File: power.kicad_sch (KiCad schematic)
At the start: 50 parts, among them J5 Ride Through, Q12 BSS138, Q3 2N7002, U2 MAX17614, U3 TVS3300DRV, U4 LM61480

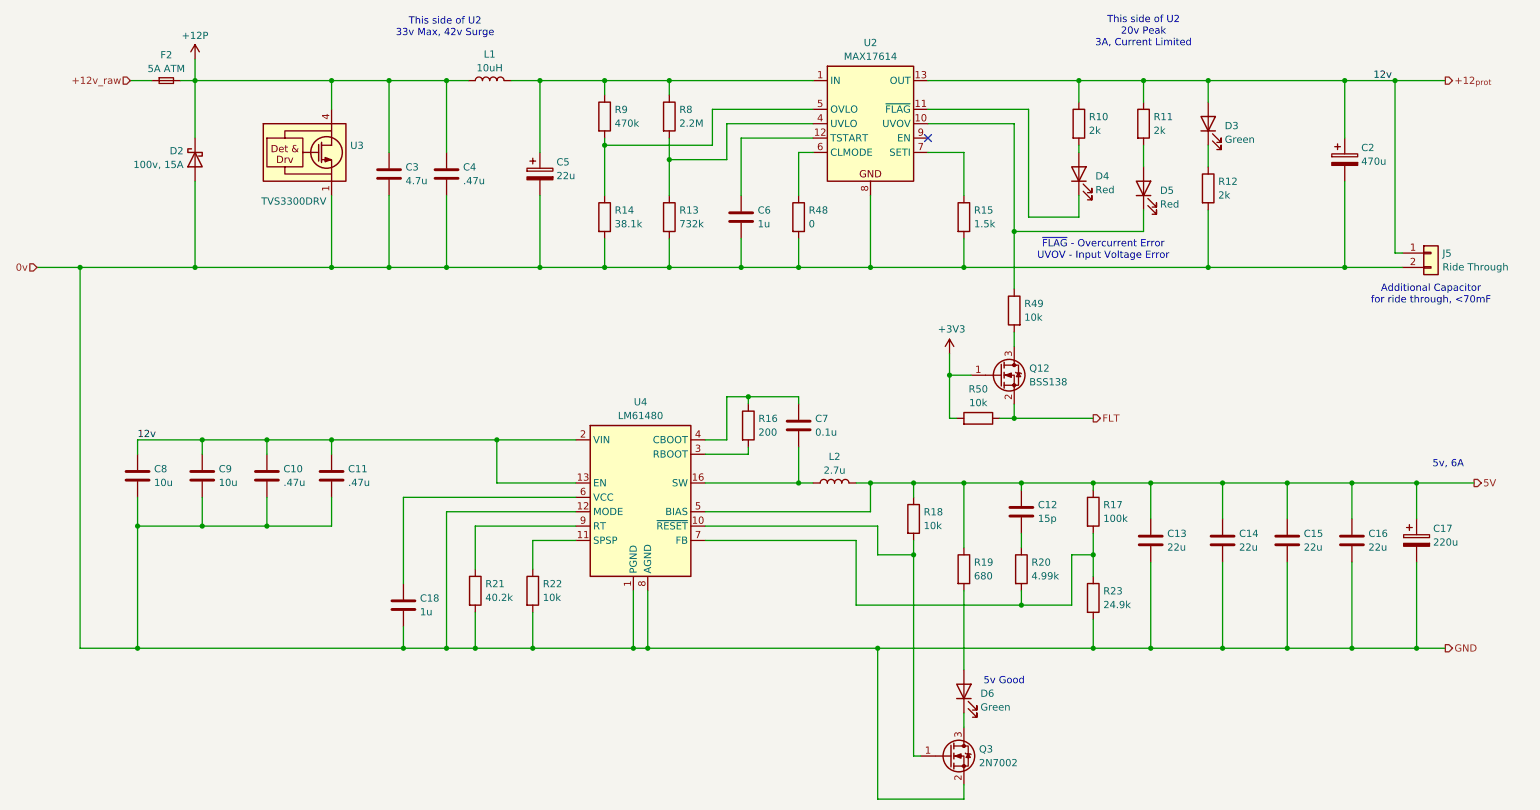
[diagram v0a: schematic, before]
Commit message: remove vf led, add en divider to 5v regulator to fix sequencing
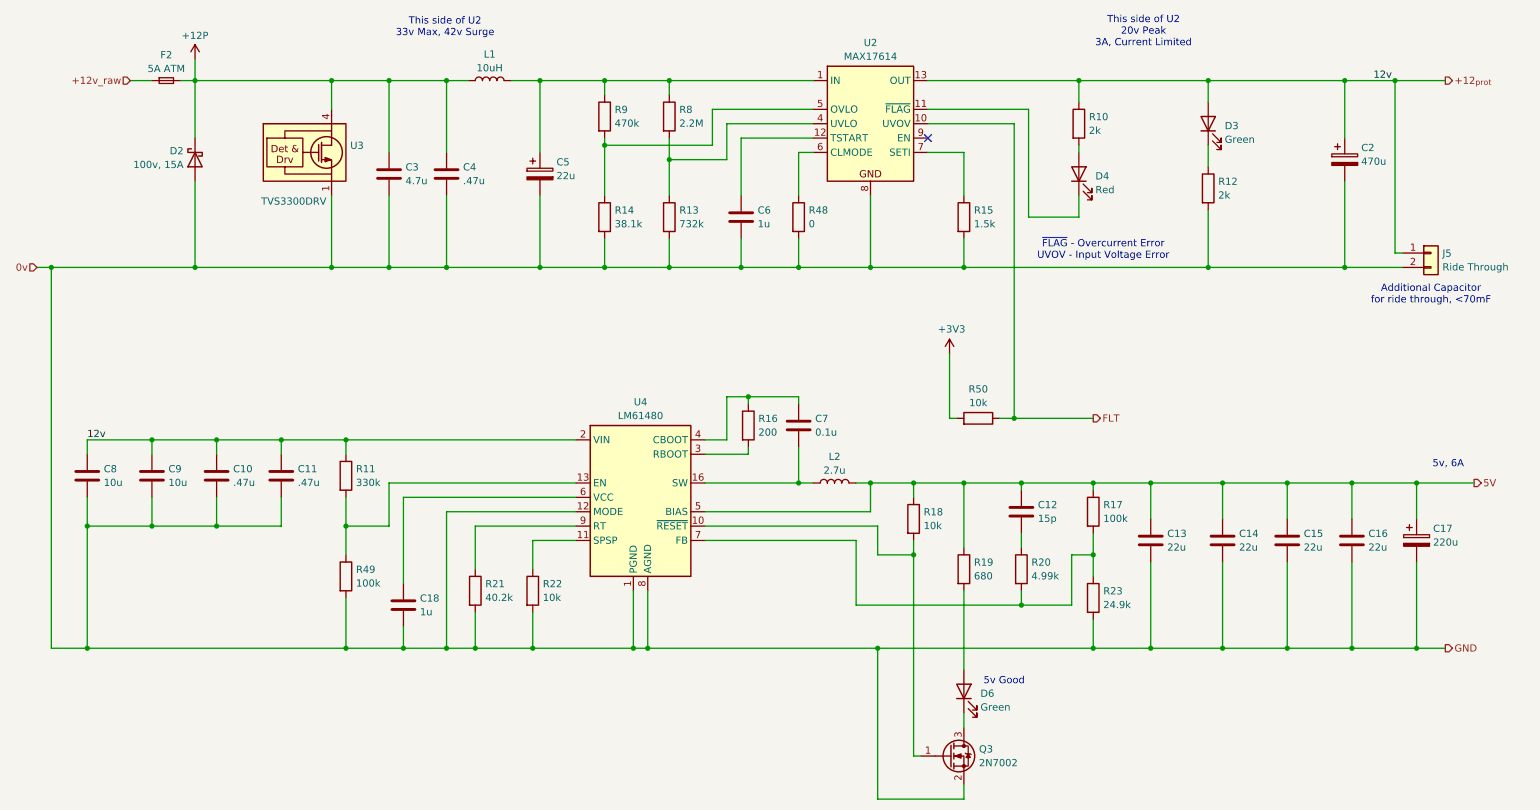
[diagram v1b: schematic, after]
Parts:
- removed D5: Red, LED_SMD:LED_0603_1608Metric, symbol Device:LED
- removed Q12: BSS138, Package_TO_SOT_SMD:SOT-23, symbol Transistor_FET:BSS138
- R11: value 2k -> 330k
- R49: value 10k -> 100k
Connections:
- net FLT: now also U2.10 (UVOV)
- net PGND: now also R49.2
- net VIN: no longer U4.13 (EN)
- net at R49.1: now also R11.2, U4.13 (EN); no longer U2.10 (UVOV)
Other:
- moved on the sheet: C10, C11, C8, C9
